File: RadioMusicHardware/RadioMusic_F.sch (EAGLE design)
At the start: 30 parts, among them X1 VERT_SD_CARD_REV2

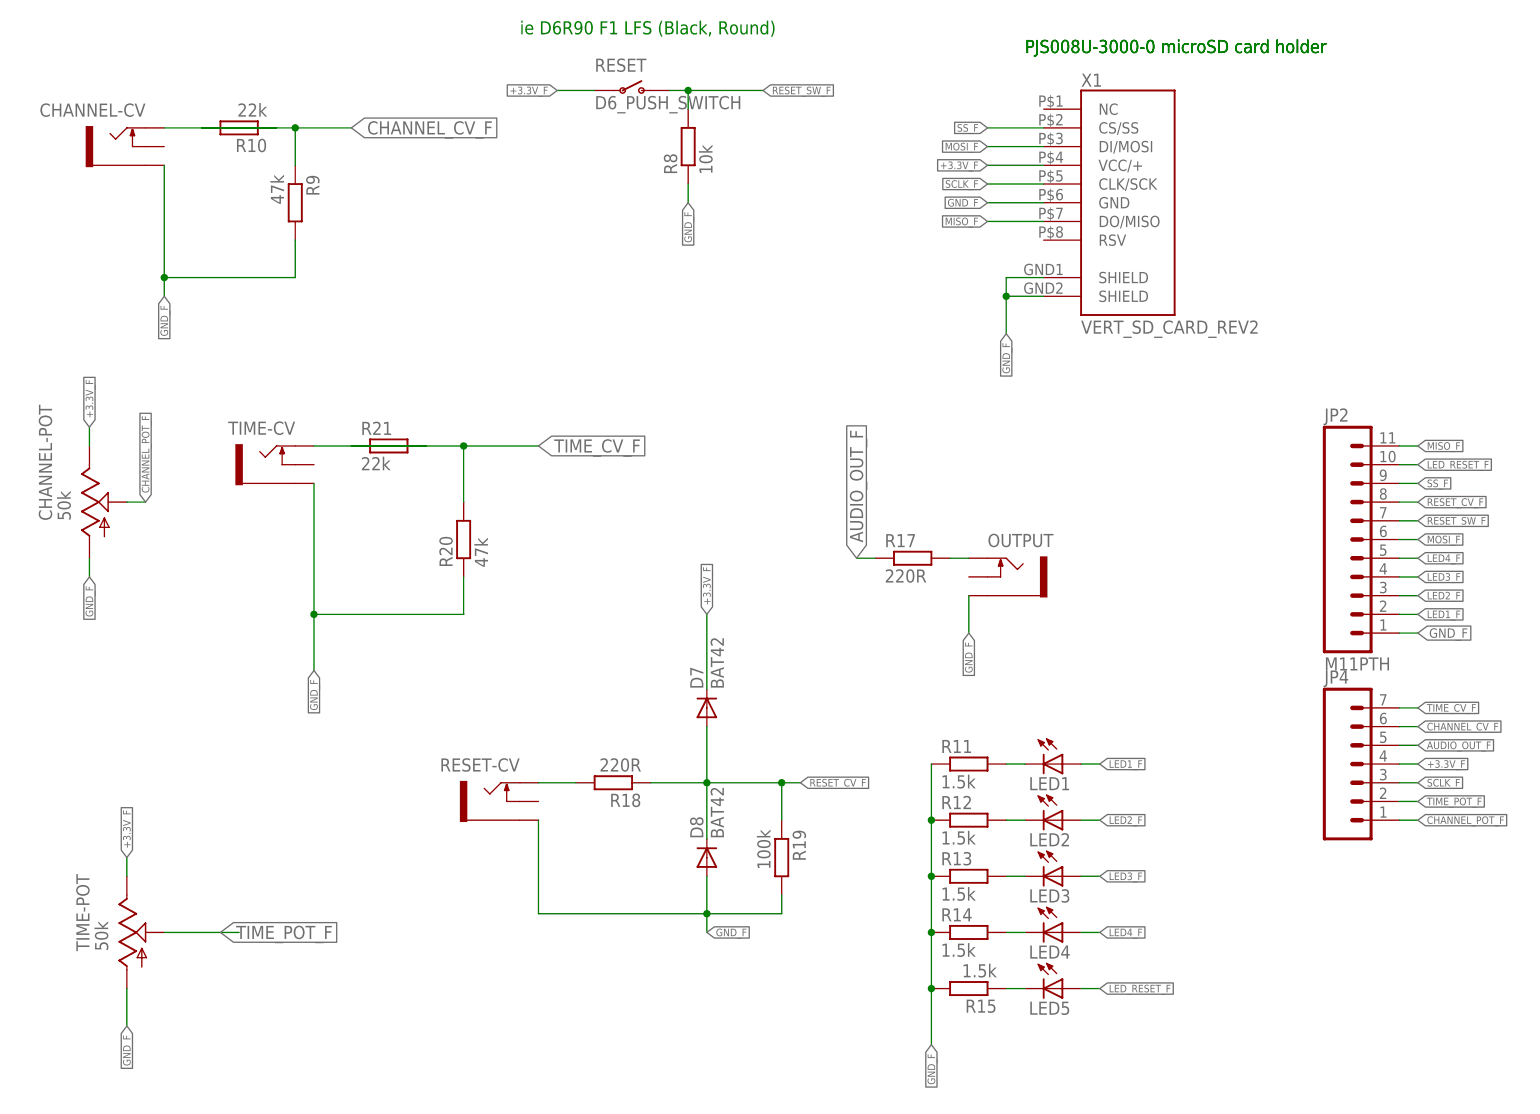
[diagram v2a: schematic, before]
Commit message: Revision 3 front and back PCBs sent to Fab
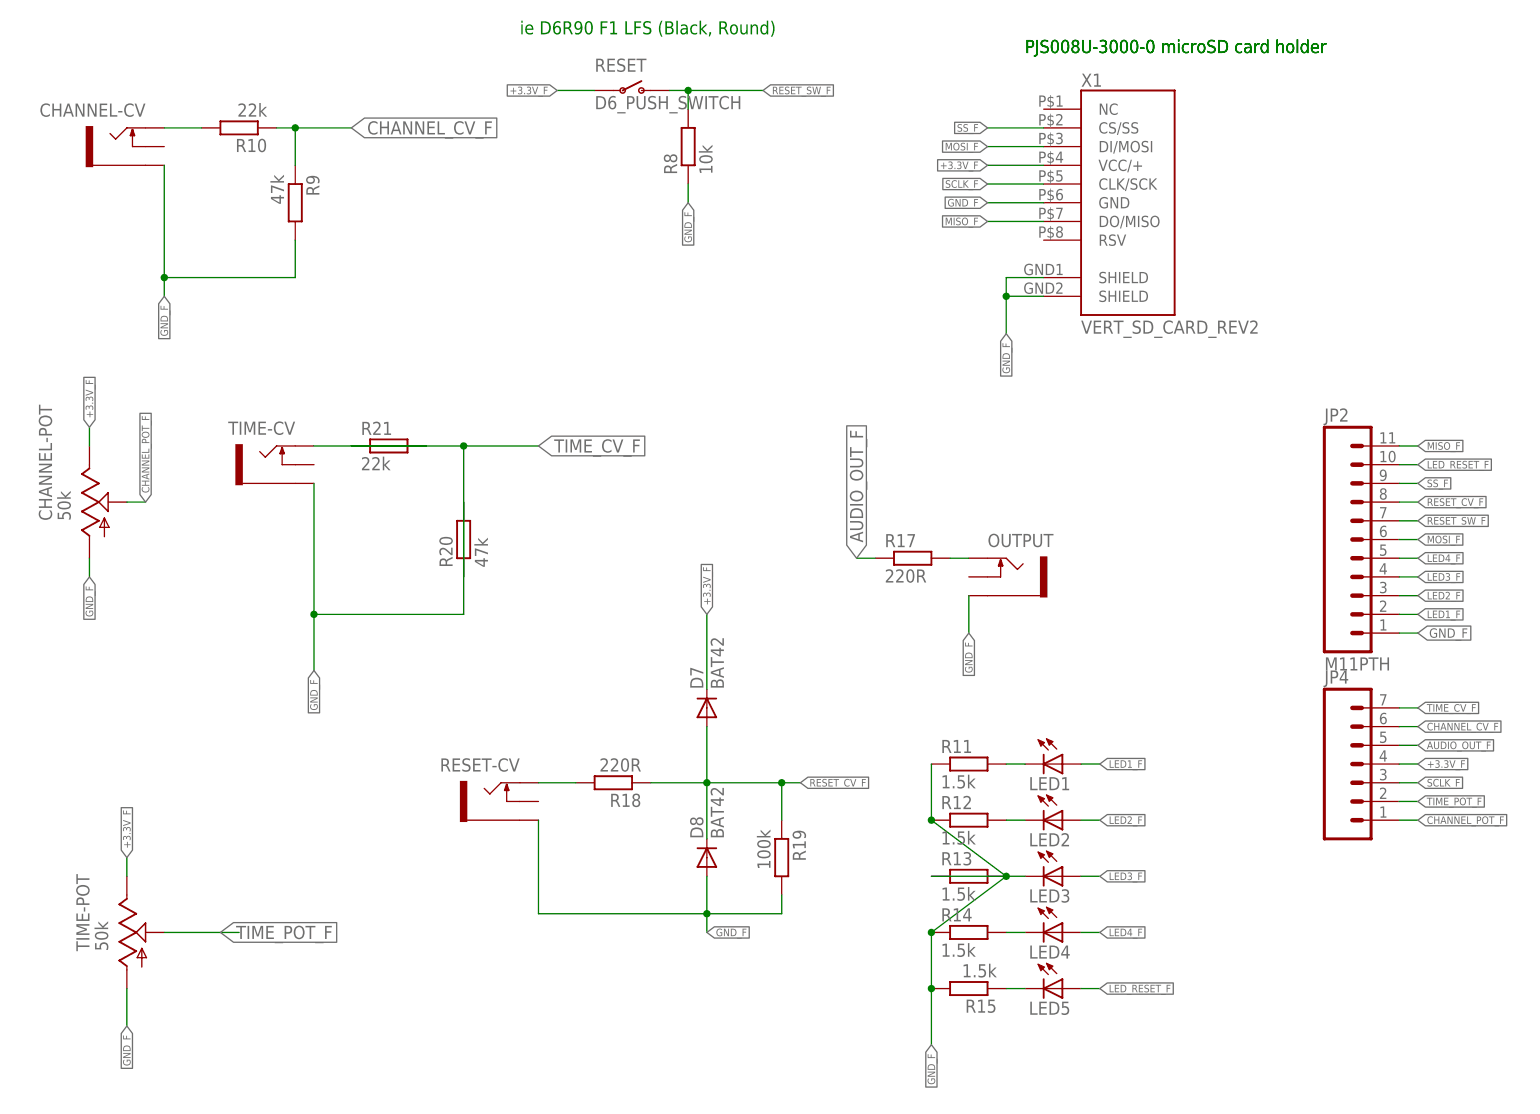
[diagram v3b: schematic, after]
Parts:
- R10, R13, R20, R21: device TomW:R-EU_STANDARD_RESISTOR -> MusicThingModular:RESISTORVERTICAL
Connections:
- net CHANNEL_CV_F: now also R10.1; no longer R10.2
- net GND_F: now also R13.2, R20.2; no longer R13.1, R20.1
- net N$1: now also R10.2; no longer R10.1
- net N$20: now also R13.1; no longer R13.2
- net TIME_CV_F: now also R20.1; no longer R20.2
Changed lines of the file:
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@@
 <part name="OUTPUT" library="MusicThingModular" deviceset="THONKICONN" device="NEW" value="THONKICONNNEW"/>
 <part name="R9" library="TomW" deviceset="R-EU_" device="STANDARD_RESISTOR" value="47k"/>
-<part name="R10" library="TomW" deviceset="R-EU_" device="STANDARD_RESISTOR" value="22k"/>
+<part name="R10" library="MusicThingModular" deviceset="RESISTOR" device="VERTICAL" value="22k"/>
 <part name="R17" library="TomW" deviceset="R-EU_" device="STANDARD_RESISTOR" value="220R"/>
 <part name="TIME-POT" library="TomW" deviceset="ALPHA-9MM" device="A" technology="F2" value="50k"/>
 <part name="TIME-CV" library="MusicThingModular" deviceset="THONKICONN" device="NEW" value="THONKICONNNEW"/>
-<part name="R20" library="TomW" deviceset="R-EU_" device="STANDARD_RESISTOR" value="47k"/>
-<part name="R21" library="TomW" deviceset="R-EU_" device="STANDARD_RESISTOR" value="22k"/>
+<part name="R20" library="MusicThingModular" deviceset="RESISTOR" device="VERTICAL" value="47k"/>
+<part name="R21" library="MusicThingModular" deviceset="RESISTOR" device="VERTICAL" value="22k"/>
 <part name="D7" library="diode" deviceset="BAT81" device="" value="BAT42"/>
 <part name="D8" library="diode" deviceset="BAT81" device="" value="BAT42"/>
@@
 <part name="R11" library="TomW" deviceset="R-EU_" device="STANDARD_RESISTOR" value="1.5k"/>
 <part name="R12" library="TomW" deviceset="R-EU_" device="STANDARD_RESISTOR" value="1.5k"/>
-<part name="R13" library="TomW" deviceset="R-EU_" device="STANDARD_RESISTOR" value="1.5k"/>
+<part name="R13" library="MusicThingModular" deviceset="RESISTOR" device="VERTICAL" value="1.5k"/>
 <part name="R14" library="TomW" deviceset="R-EU_" device="STANDARD_RESISTOR" value="1.5k"/>
 <part name="X1" library="TomW" deviceset="VERT_SD_CARD_REV2" device=""/>
@@
 <segment>
 <pinref part="LED3" gate="G$1" pin="C"/>
-<pinref part="R13" gate="G$1" pin="2"/>
-<wire x1="149.86" y1="30.48" x2="152.4" y2="30.48" width="0.1524" layer="91"/>
+<pinref part="R13" gate="G$1" pin="1"/>
+<wire x1="139.7" y1="30.48" x2="152.4" y2="30.48" width="0.1524" layer="91"/>
 </segment>
 </net>
@@
 <wire x1="55.88" y1="58.42" x2="55.88" y2="66.04" width="0.1524" layer="91"/>
 <label x="55.88" y="58.42" size="1.016" layer="95" rot="R270" xref="yes"/>
-<pinref part="R20" gate="G$1" pin="1"/>
+<pinref part="R20" gate="G$1" pin="2"/>
 <wire x1="55.88" y1="66.04" x2="55.88" y2="83.82" width="0.1524" layer="91"/>
-<wire x1="76.2" y1="71.12" x2="76.2" y2="66.04" width="0.1524" layer="91"/>
+<wire x1="76.2" y1="81.28" x2="76.2" y2="66.04" width="0.1524" layer="91"/>
 <wire x1="76.2" y1="66.04" x2="55.88" y2="66.04" width="0.1524" layer="91"/>
 <junction x="55.88" y="66.04"/>
@@
 <pinref part="R11" gate="G$1" pin="1"/>
 <pinref part="R12" gate="G$1" pin="1"/>
-<wire x1="139.7" y1="38.1" x2="139.7" y2="30.48" width="0.1524" layer="91"/>
+<wire x1="139.7" y1="38.1" x2="149.86" y2="30.48" width="0.1524" layer="91"/>
 <junction x="139.7" y="38.1"/>
-<pinref part="R13" gate="G$1" pin="1"/>
-<wire x1="139.7" y1="30.48" x2="139.7" y2="22.86" width="0.1524" layer="91"/>
-<junction x="139.7" y="30.48"/>
+<pinref part="R13" gate="G$1" pin="2"/>
+<wire x1="149.86" y1="30.48" x2="139.7" y2="22.86" width="0.1524" layer="91"/>
+<junction x="149.86" y="30.48"/>
 <pinref part="R14" gate="G$1" pin="1"/>
 <wire x1="139.7" y1="22.86" x2="139.7" y2="15.24" width="0.1524" layer="91"/>
@@
 </segment>
 <segment>
-<pinref part="R10" gate="G$1" pin="2"/>
-<wire x1="40.64" y1="132.08" x2="53.34" y2="132.08" width="0.1524" layer="91"/>
+<pinref part="R10" gate="G$1" pin="1"/>
+<wire x1="50.8" y1="132.08" x2="53.34" y2="132.08" width="0.1524" layer="91"/>
 <pinref part="R9" gate="G$1" pin="1"/>
 <wire x1="53.34" y1="132.08" x2="60.96" y2="132.08" width="0.1524" layer="91"/>
@@
 <pinref part="R21" gate="G$1" pin="1"/>
 <wire x1="60.96" y1="88.9" x2="76.2" y2="88.9" width="0.1524" layer="91"/>
-<pinref part="R20" gate="G$1" pin="2"/>
+<pinref part="R20" gate="G$1" pin="1"/>
 <wire x1="76.2" y1="88.9" x2="86.36" y2="88.9" width="0.1524" layer="91"/>
-<wire x1="76.2" y1="81.28" x2="76.2" y2="88.9" width="0.1524" layer="91"/>
+<wire x1="76.2" y1="71.12" x2="76.2" y2="88.9" width="0.1524" layer="91"/>
 <junction x="76.2" y="88.9"/>
 <label x="86.36" y="88.9" size="1.778" layer="95" xref="yes"/>
@@
 <segment>
 <pinref part="CHANNEL-CV" gate="G$1" pin="TIP"/>
-<pinref part="R10" gate="G$1" pin="1"/>
-<wire x1="50.8" y1="132.08" x2="35.56" y2="132.08" width="0.1524" layer="91"/>
-</segment>
-</net>
+<pinref part="R10" gate="G$1" pin="2"/>
+<wire x1="40.64" y1="132.08" x2="35.56" y2="132.08" width="0.1524" layer="91"/>
+</segment>
+</net>

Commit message: 3.1 Hardware Finalised
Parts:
- R11, R12, R14, R15, R17, R18, R19, R8, R9: device TomW:R-EU_STANDARD_RESISTOR -> MusicThingModular:RESISTOR7MM
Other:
- moved on the sheet: R13, R20, R21
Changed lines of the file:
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@@
 <?xml version="1.0" encoding="utf-8"?>
 <!DOCTYPE eagle SYSTEM "eagle.dtd">
-<eagle version="7.4.0">
+<eagle version="7.2.0">
 <drawing>
 <settings>
@@
 <part name="RESET-CV" library="MusicThingModular" deviceset="THONKICONN" device="NEW" value="THONKICONNNEW"/>
 <part name="OUTPUT" library="MusicThingModular" deviceset="THONKICONN" device="NEW" value="THONKICONNNEW"/>
-<part name="R9" library="TomW" deviceset="R-EU_" device="STANDARD_RESISTOR" value="47k"/>
+<part name="R9" library="MusicThingModular" deviceset="RESISTOR" device="7MM" value="47k"/>
 <part name="R10" library="MusicThingModular" deviceset="RESISTOR" device="VERTICAL" value="22k"/>
-<part name="R17" library="TomW" deviceset="R-EU_" device="STANDARD_RESISTOR" value="220R"/>
+<part name="R17" library="MusicThingModular" deviceset="RESISTOR" device="7MM" value="220R"/>
 <part name="TIME-POT" library="TomW" deviceset="ALPHA-9MM" device="A" technology="F2" value="50k"/>
 <part name="TIME-CV" library="MusicThingModular" deviceset="THONKICONN" device="NEW" value="THONKICONNNEW"/>
@@
 <part name="D7" library="diode" deviceset="BAT81" device="" value="BAT42"/>
 <part name="D8" library="diode" deviceset="BAT81" device="" value="BAT42"/>
-<part name="R19" library="TomW" deviceset="R-EU_" device="STANDARD_RESISTOR" value="100k"/>
-<part name="R18" library="TomW" deviceset="R-EU_" device="STANDARD_RESISTOR" value="220R"/>
+<part name="R19" library="MusicThingModular" deviceset="RESISTOR" device="7MM" value="100k"/>
+<part name="R18" library="MusicThingModular" deviceset="RESISTOR" device="7MM" value="220R"/>
 <part name="RESET" library="TomW" deviceset="D6_PUSH_SWITCH" device="" value="D6_PUSH_SWITCH"/>
-<part name="R8" library="TomW" deviceset="R-EU_" device="STANDARD_RESISTOR" value="10k"/>
+<part name="R8" library="MusicThingModular" deviceset="RESISTOR" device="7MM" value="10k"/>
 <part name="LED1" library="TomW" deviceset="LED" device="3MM"/>
 <part name="LED2" library="TomW" deviceset="LED" device="3MM"/>
 <part name="LED3" library="TomW" deviceset="LED" device="3MM"/>
 <part name="LED4" library="TomW" deviceset="LED" device="3MM"/>
-<part name="R11" library="TomW" deviceset="R-EU_" device="STANDARD_RESISTOR" value="1.5k"/>
-<part name="R12" library="TomW" deviceset="R-EU_" device="STANDARD_RESISTOR" value="1.5k"/>
+<part name="R11" library="MusicThingModular" deviceset="RESISTOR" device="7MM" value="1.5k"/>
+<part name="R12" library="MusicThingModular" deviceset="RESISTOR" device="7MM" value="1.5k"/>
 <part name="R13" library="MusicThingModular" deviceset="RESISTOR" device="VERTICAL" value="1.5k"/>
-<part name="R14" library="TomW" deviceset="R-EU_" device="STANDARD_RESISTOR" value="1.5k"/>
+<part name="R14" library="MusicThingModular" deviceset="RESISTOR" device="7MM" value="1.5k"/>
 <part name="X1" library="TomW" deviceset="VERT_SD_CARD_REV2" device=""/>
 <part name="LED5" library="TomW" deviceset="LED" device="3MM"/>
-<part name="R15" library="TomW" deviceset="R-EU_" device="STANDARD_RESISTOR" value="1.5k"/>
+<part name="R15" library="MusicThingModular" deviceset="RESISTOR" device="7MM" value="1.5k"/>
 <part name="JP2" library="SparkFun-Connectors" deviceset="M11" device="PTH" value="M11PTH"/>
 <part name="JP4" library="SparkFun-Connectors" deviceset="M07" device=""/>
@@
 <instance part="TIME-POT" gate="G$1" x="30.48" y="22.86"/>
 <instance part="TIME-CV" gate="G$1" x="50.8" y="86.36" rot="MR0"/>
-<instance part="R20" gate="G$1" x="76.2" y="76.2" rot="R90"/>
-<instance part="R21" gate="G$1" x="66.04" y="88.9"/>
+<instance part="R20" gate="G$1" x="76.2" y="76.2" rot="R270"/>
+<instance part="R21" gate="G$1" x="66.04" y="88.9" rot="R180"/>
 <instance part="D7" gate="1" x="109.22" y="53.34" rot="R90"/>
 <instance part="D8" gate="1" x="109.22" y="33.02" rot="R90"/>
@@
 <instance part="R11" gate="G$1" x="144.78" y="45.72"/>
 <instance part="R12" gate="G$1" x="144.78" y="38.1"/>
-<instance part="R13" gate="G$1" x="144.78" y="30.48"/>
+<instance part="R13" gate="G$1" x="144.78" y="30.48" rot="R180"/>
 <instance part="R14" gate="G$1" x="144.78" y="22.86"/>
 <instance part="X1" gate="G$1" x="162.56" y="121.92"/>
@@
 <pinref part="LED3" gate="G$1" pin="C"/>
 <pinref part="R13" gate="G$1" pin="1"/>
-<wire x1="139.7" y1="30.48" x2="152.4" y2="30.48" width="0.1524" layer="91"/>
+<wire x1="149.86" y1="30.48" x2="152.4" y2="30.48" width="0.1524" layer="91"/>
 </segment>
 </net>
@@
 <pinref part="R20" gate="G$1" pin="2"/>
 <wire x1="55.88" y1="66.04" x2="55.88" y2="83.82" width="0.1524" layer="91"/>
-<wire x1="76.2" y1="81.28" x2="76.2" y2="66.04" width="0.1524" layer="91"/>
+<wire x1="76.2" y1="71.12" x2="76.2" y2="66.04" width="0.1524" layer="91"/>
 <wire x1="76.2" y1="66.04" x2="55.88" y2="66.04" width="0.1524" layer="91"/>
 <junction x="55.88" y="66.04"/>
@@
 <pinref part="R11" gate="G$1" pin="1"/>
 <pinref part="R12" gate="G$1" pin="1"/>
-<wire x1="139.7" y1="38.1" x2="149.86" y2="30.48" width="0.1524" layer="91"/>
+<wire x1="139.7" y1="38.1" x2="139.7" y2="30.48" width="0.1524" layer="91"/>
 <junction x="139.7" y="38.1"/>
 <pinref part="R13" gate="G$1" pin="2"/>
-<wire x1="149.86" y1="30.48" x2="139.7" y2="22.86" width="0.1524" layer="91"/>
-<junction x="149.86" y="30.48"/>
+<wire x1="139.7" y1="30.48" x2="139.7" y2="22.86" width="0.1524" layer="91"/>
+<junction x="139.7" y="30.48"/>
 <pinref part="R14" gate="G$1" pin="1"/>
 <wire x1="139.7" y1="22.86" x2="139.7" y2="15.24" width="0.1524" layer="91"/>
@@
 <segment>
 <pinref part="R21" gate="G$1" pin="1"/>
-<wire x1="60.96" y1="88.9" x2="76.2" y2="88.9" width="0.1524" layer="91"/>
+<wire x1="71.12" y1="88.9" x2="76.2" y2="88.9" width="0.1524" layer="91"/>
 <pinref part="R20" gate="G$1" pin="1"/>
 <wire x1="76.2" y1="88.9" x2="86.36" y2="88.9" width="0.1524" layer="91"/>
-<wire x1="76.2" y1="71.12" x2="76.2" y2="88.9" width="0.1524" layer="91"/>
+<wire x1="76.2" y1="81.28" x2="76.2" y2="88.9" width="0.1524" layer="91"/>
 <junction x="76.2" y="88.9"/>
 <label x="86.36" y="88.9" size="1.778" layer="95" xref="yes"/>
@@
 <pinref part="TIME-CV" gate="G$1" pin="TIP"/>
 <pinref part="R21" gate="G$1" pin="2"/>
-<wire x1="71.12" y1="88.9" x2="55.88" y2="88.9" width="0.1524" layer="91"/>
-</segment>
-</net>
+<wire x1="60.96" y1="88.9" x2="55.88" y2="88.9" width="0.1524" layer="91"/>
+</segment>
+</net>
